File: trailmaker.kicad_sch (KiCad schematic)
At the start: 13 parts, among them SW1 SW_Push, SW2 SW_Push, SW3 SW_Push, SW4 SW_Push, U1 XIAO-RP2040-DIP

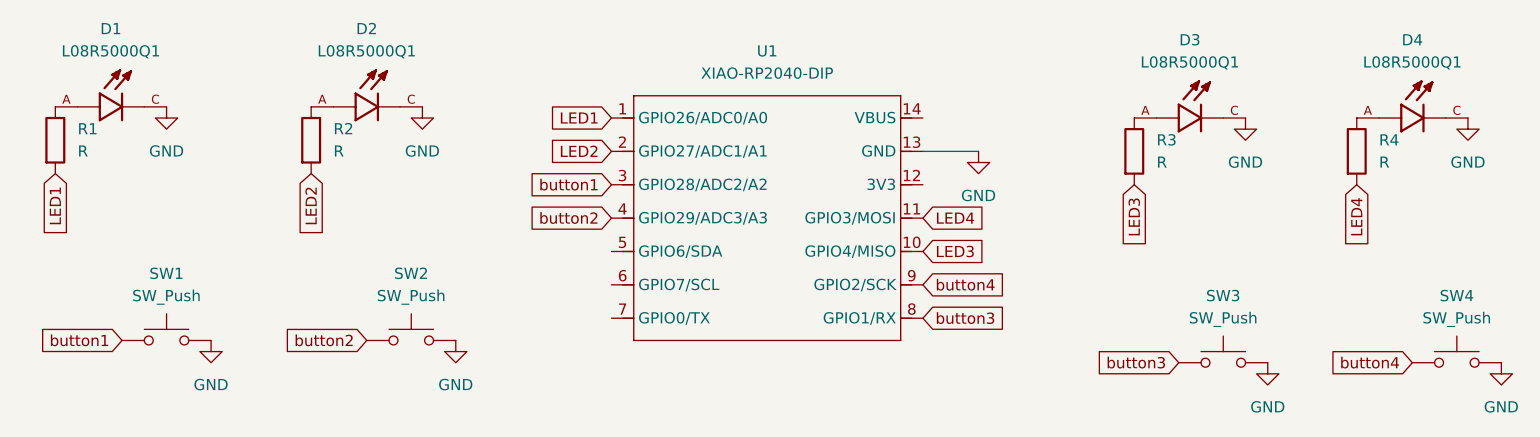
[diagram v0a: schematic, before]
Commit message: created PCB layout and Arduino code
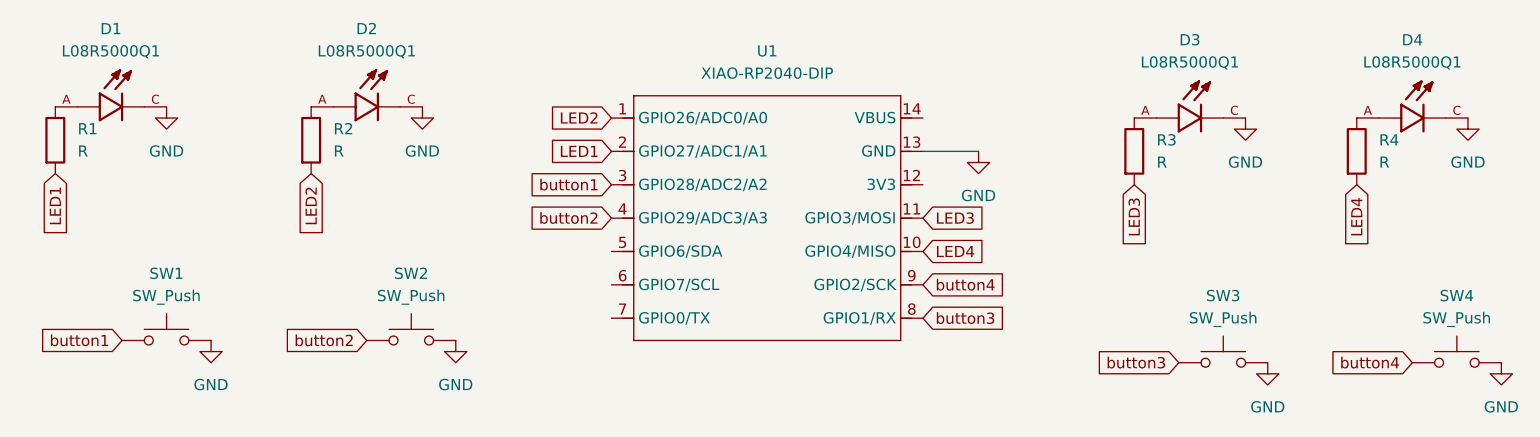
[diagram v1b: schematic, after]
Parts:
- SW1, SW2, SW3, SW4: footprint Button_Switch_Keyboard:SW_Cherry_MX_1.00u_PCB -> footprints:SW_Cherry_MX_1.00u_PCB_Rubey
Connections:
- net LED1: now also U1.2 (GPIO27/ADC1/A1); no longer U1.1 (GPIO26/ADC0/A0)
- net LED2: now also U1.1 (GPIO26/ADC0/A0); no longer U1.2 (GPIO27/ADC1/A1)
- net LED3: now also U1.11 (GPIO3/MOSI); no longer U1.10 (GPIO4/MISO)
- net LED4: now also U1.10 (GPIO4/MISO); no longer U1.11 (GPIO3/MOSI)
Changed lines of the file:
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@@
 		)
 	)
-	(global_label "LED3"
+	(global_label "LED4"
 		(shape input)
 		(at 146.05 90.17 0)
@@
 		)
 	)
-	(global_label "LED2"
+	(global_label "LED1"
 		(shape input)
 		(at 110.49 78.74 180)
@@
 		)
 	)
-	(global_label "LED4"
+	(global_label "LED3"
 		(shape input)
 		(at 146.05 86.36 0)
@@
 		)
 	)
-	(global_label "LED1"
+	(global_label "LED2"
 		(shape input)
 		(at 110.49 74.93 180)
@@
 			)
 		)
-		(property "Footprint" "Button_Switch_Keyboard:SW_Cherry_MX_1.00u_PCB"
+		(property "Footprint" "footprints:SW_Cherry_MX_1.00u_PCB_Rubey"
 			(at 59.69 95.25 0)
 			(effects
@@
 			)
 		)
-		(property "Footprint" "Button_Switch_Keyboard:SW_Cherry_MX_1.00u_PCB"
+		(property "Footprint" "footprints:SW_Cherry_MX_1.00u_PCB_Rubey"
 			(at 207.01 97.79 0)
 			(effects
@@
 			)
 		)
-		(property "Footprint" "Button_Switch_Keyboard:SW_Cherry_MX_1.00u_PCB"
+		(property "Footprint" "footprints:SW_Cherry_MX_1.00u_PCB_Rubey"
 			(at 87.63 95.25 0)
 			(effects
@@
 			)
 		)
-		(property "Footprint" "Button_Switch_Keyboard:SW_Cherry_MX_1.00u_PCB"
+		(property "Footprint" "footprints:SW_Cherry_MX_1.00u_PCB_Rubey"
 			(at 180.34 97.79 0)
 			(effects

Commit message: Code bug fixing and PCB finalization
Added silkscreen to PCB and exported gerber and dril file for JLC PCB
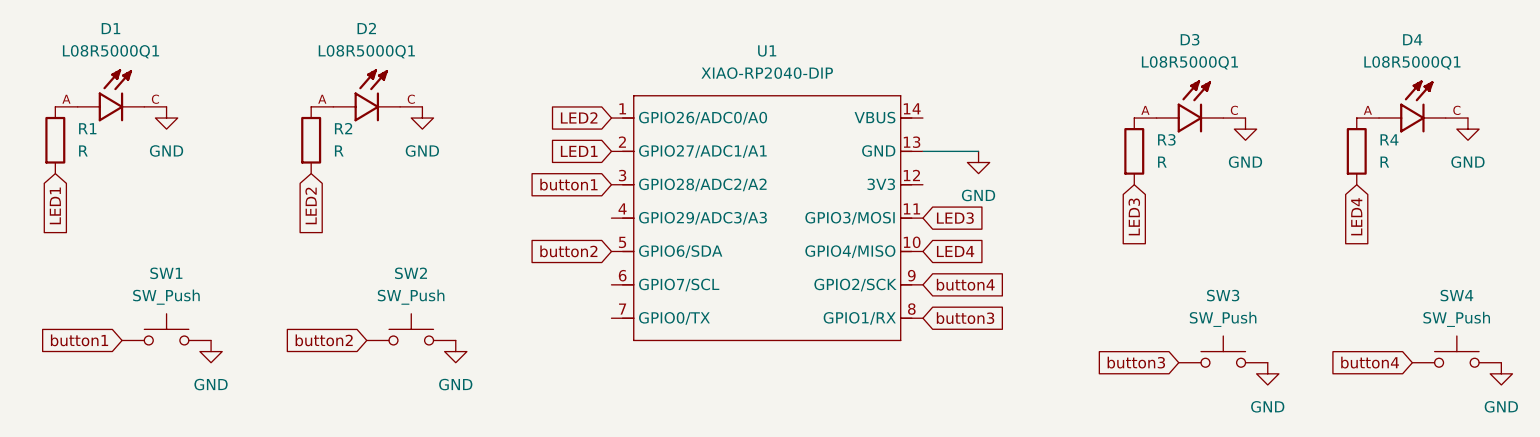
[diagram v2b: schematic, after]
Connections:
- net button2: now also U1.5 (GPIO6/SDA); no longer U1.4 (GPIO29/ADC3/A3)
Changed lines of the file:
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@@
+		)
+	)
+	(global_label "button3"
+		(shape input)
+		(at 146.05 97.79 0)
+		(fields_autoplaced yes)
+		(effects
+			(font
+				(size 1.27 1.27)
+			)
+			(justify left)
+		)
+		(property "Intersheetrefs" "${INTERSHEET_REFS}"
+			(at 146.05 108.0321 90)
+			(effects
+				(font
+					(size 1.27 1.27)
+				)
+				(justify right)
+				(hide yes)
+			)
+		)
+	)
+	(global_label "LED1"
+		(shape input)
+		(at 110.49 78.74 180)
+		(fields_autoplaced yes)
+		(effects
+			(font
+				(size 1.27 1.27)
+			)
+			(justify right)
+		)
+		(property "Intersheetrefs" "${INTERSHEET_REFS}"
+			(at 102.8482 78.74 0)
+			(effects
+				(font
+					(size 1.27 1.27)
+				)
+				(justify right)
+				(hide yes)
+			)
+		)
+	)
+	(global_label "LED1"
+		(shape input)
+		(at 46.99 81.28 270)
+		(fields_autoplaced yes)
+		(effects
+			(font
+				(size 1.27 1.27)
+			)
+			(justify right)
+		)
+		(property "Intersheetrefs" "${INTERSHEET_REFS}"
+			(at 46.99 88.9218 90)
+			(effects
+				(font
+					(size 1.27 1.27)
+				)
+				(justify right)
+				(hide yes)
+			)
+		)
+	)
+	(global_label "button3"
+		(shape input)
+		(at 175.26 102.87 180)
+		(fields_autoplaced yes)
+		(effects
+			(font
+				(size 1.27 1.27)
+			)
+			(justify right)
+		)
+		(property "Intersheetrefs" "${INTERSHEET_REFS}"
+			(at 165.0179 102.87 0)
+			(effects
+				(font
+					(size 1.27 1.27)
+				)
+				(justify right)
+				(hide yes)
+			)
+		)
+	)
+	(global_label "button4"
+		(shape input)
+		(at 146.05 93.98 0)
+		(fields_autoplaced yes)
+		(effects
+			(font
+				(size 1.27 1.27)
+			)
+			(justify left)
+		)
+		(property "Intersheetrefs" "${INTERSHEET_REFS}"
+			(at 156.2921 93.98 0)
+			(effects
+				(font
+					(size 1.27 1.27)
+				)
+				(justify left)
+				(hide yes)
+			)
+		)
+	)
+	(global_label "LED2"
+		(shape input)
+		(at 76.2 81.28 270)
+		(fields_autoplaced yes)
+		(effects
+			(font
+				(size 1.27 1.27)
+			)
+			(justify right)
+		)
+		(property "Intersheetrefs" "${INTERSHEET_REFS}"
+			(at 76.2 88.9218 90)
+			(effects
+				(font
+					(size 1.27 1.27)
+				)
+				(justify right)
+				(hide yes)
+			)
+		)
+	)
+	(global_label "button1"
+		(shape input)
+		(at 110.49 82.55 180)
+		(fields_autoplaced yes)
+		(effects
+			(font
+				(size 1.27 1.27)
+			)
+			(justify right)
+		)
+		(property "Intersheetrefs" "${INTERSHEET_REFS}"
+			(at 100.2479 82.55 0)
+			(effects
+				(font
+					(size 1.27 1.27)
+				)
+				(justify right)
+				(hide yes)
+			)
+		)
+	)
+	(global_label "LED3"
+		(shape input)
+		(at 146.05 86.36 0)
+		(fields_autoplaced yes)
+		(effects
+			(font
+				(size 1.27 1.27)
+			)
+			(justify left)
+		)
+		(property "Intersheetrefs" "${INTERSHEET_REFS}"
+			(at 153.6918 86.36 0)
+			(effects
+				(font
+					(size 1.27 1.27)
+				)
+				(justify left)
+				(hide yes)
+			)
+		)
+	)
+	(global_label "LED3"
+		(shape input)
+		(at 170.18 82.55 270)
+		(fields_autoplaced yes)
+		(effects
+			(font
+				(size 1.27 1.27)
+			)
+			(justify right)
+		)
+		(property "Intersheetrefs" "${INTERSHEET_REFS}"
+			(at 170.18 90.1918 90)
+			(effects
+				(font
+					(size 1.27 1.27)
+				)
+				(justify right)
+				(hide yes)
+			)
 		)
 	)
 	(global_label "button2"
 		(shape input)
-		(at 110.49 86.36 180)
-		(fields_autoplaced yes)
-		(effects
-			(font
-				(size 1.27 1.27)
-			)
-			(justify right)
-		)
-		(property "Intersheetrefs" "${INTERSHEET_REFS}"
-			(at 100.2479 86.36 0)
-			(effects
-				(font
-					(size 1.27 1.27)
-				)
-				(justify right)
-				(hide yes)
-			)
-		)
-	)
-	(global_label "button3"
-		(shape input)
-		(at 146.05 97.79 0)
-		(fields_autoplaced yes)
-		(effects
-			(font
-				(size 1.27 1.27)
-			)
-			(justify left)
-		)
-		(property "Intersheetrefs" "${INTERSHEET_REFS}"
-			(at 146.05 108.0321 90)
-			(effects
-				(font
-					(size 1.27 1.27)
-				)
-				(justify right)
-				(hide yes)
-			)
-		)
-	)
-	(global_label "LED1"
-		(shape input)
-		(at 110.49 78.74 180)
-		(fields_autoplaced yes)
-		(effects
-			(font
-				(size 1.27 1.27)
-			)
-			(justify right)
-		)
-		(property "Intersheetrefs" "${INTERSHEET_REFS}"
-			(at 102.8482 78.74 0)
-			(effects
-				(font
-					(size 1.27 1.27)
-				)
-				(justify right)
-				(hide yes)
-			)
-		)
-	)
-	(global_label "LED1"
-		(shape input)
-		(at 46.99 81.28 270)
-		(fields_autoplaced yes)
-		(effects
-			(font
-				(size 1.27 1.27)
-			)
-			(justify right)
-		)
-		(property "Intersheetrefs" "${INTERSHEET_REFS}"
-			(at 46.99 88.9218 90)
-			(effects
-				(font
-					(size 1.27 1.27)
-				)
-				(justify right)
-				(hide yes)
-			)
-		)
-	)
-	(global_label "button3"
-		(shape input)
-		(at 175.26 102.87 180)
-		(fields_autoplaced yes)
-		(effects
-			(font
-				(size 1.27 1.27)
-			)
-			(justify right)
-		)
-		(property "Intersheetrefs" "${INTERSHEET_REFS}"
-			(at 165.0179 102.87 0)
-			(effects
-				(font
-					(size 1.27 1.27)
-				)
-				(justify right)
-				(hide yes)
-			)
-		)
-	)
-	(global_label "button4"
-		(shape input)
-		(at 146.05 93.98 0)
-		(fields_autoplaced yes)
-		(effects
-			(font
-				(size 1.27 1.27)
-			)
-			(justify left)
-		)
-		(property "Intersheetrefs" "${INTERSHEET_REFS}"
-			(at 156.2921 93.98 0)
-			(effects
-				(font
-					(size 1.27 1.27)
-				)
-				(justify left)
-				(hide yes)
-			)
-		)
-	)
-	(global_label "LED2"
-		(shape input)
-		(at 76.2 81.28 270)
-		(fields_autoplaced yes)
-		(effects
-			(font
-				(size 1.27 1.27)
-			)
-			(justify right)
-		)
-		(property "Intersheetrefs" "${INTERSHEET_REFS}"
-			(at 76.2 88.9218 90)
-			(effects
-				(font
-					(size 1.27 1.27)
-				)
-				(justify right)
-				(hide yes)
-			)
-		)
-	)
-	(global_label "button1"
-		(shape input)
-		(at 110.49 82.55 180)
-		(fields_autoplaced yes)
-		(effects
-			(font
-				(size 1.27 1.27)
-			)
-			(justify right)
-		)
-		(property "Intersheetrefs" "${INTERSHEET_REFS}"
-			(at 100.2479 82.55 0)
-			(effects
-				(font
-					(size 1.27 1.27)
-				)
-				(justify right)
-				(hide yes)
-			)
-		)
-	)
-	(global_label "LED3"
-		(shape input)
-		(at 146.05 86.36 0)
-		(fields_autoplaced yes)
-		(effects
-			(font
-				(size 1.27 1.27)
-			)
-			(justify left)
-		)
-		(property "Intersheetrefs" "${INTERSHEET_REFS}"
-			(at 153.6918 86.36 0)
-			(effects
-				(font
-					(size 1.27 1.27)
-				)
-				(justify left)
-				(hide yes)
-			)
-		)
-	)
-	(global_label "LED3"
-		(shape input)
-		(at 170.18 82.55 270)
-		(fields_autoplaced yes)
-		(effects
-			(font
-				(size 1.27 1.27)
-			)
-			(justify right)
-		)
-		(property "Intersheetrefs" "${INTERSHEET_REFS}"
-			(at 170.18 90.1918 90)
-			(effects
-				(font
+		(at 110.49 90.17 180)
+		(fields_autoplaced yes)
+		(effects
+			(font
+				(size 1.27 1.27)
+			)
+			(justify right)
+		)
+		(property "Intersheetrefs" "${INTERSHEET_REFS}"
+			(at 100.2479 90.17 0)
+			(effects
+				(font
